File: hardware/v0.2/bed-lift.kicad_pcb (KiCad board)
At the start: 4 copper layers, 175 x 40 mm, 113 parts, among them J1 SM04B-SRSS-TB, J10 S4B-XH-A, J11 S4B-XH-A, J12 S4B-XH-A, J13 S4B-XH-A, J2 S2P-VH, J3 SM04B-SRSS-TB, J4 TC2030-NL, J5 PH1-06-UA, J6 S3B-XH-A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

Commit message: Finalize for production
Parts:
- added TH1: JLCPCB_PCBA_Tooling_Hole, Generic:JLCPCB_PCBA_Tooling_Hole, F.Cu at (196.5, 61.8)
- added TH1: JLCPCB_PCBA_Tooling_Hole, Generic:JLCPCB_PCBA_Tooling_Hole, F.Cu at (36.5, 98.8)
- added TH1: JLCPCB_PCBA_Tooling_Hole, Generic:JLCPCB_PCBA_Tooling_Hole, F.Cu at (202.5, 92.8)
- added TH1: JLCPCB_PCBA_Tooling_Hole, Generic:JLCPCB_PCBA_Tooling_Hole, F.Cu at (61.8, 61.8)
- moved C1 6.75 mm to (39.0, 78.0)
- moved C2 6.75 mm to (42.5, 78.0)
- moved C7 2.00 mm to (47.8, 70.5)
- moved U2 1.25 mm to (40.8, 74.0), turned to 180 degrees
- moved R1 0.50 mm to (47.8, 74.8), turned to 90 degrees
- moved R2 0.50 mm to (45.8, 74.8), turned to 90 degrees
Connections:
- U2 pad 1: /BUS_3V3 -> +3.3V
- U2 pad 2: /BUS_SDA -> /I2C1_SDA
- U2 pad 3: /BUS_SCL -> /I2C1_SCL
- U2 pad 4: /BUS_GND -> GND
- U2 pad 5: GND -> /BUS_GND
- U2 pad 6: /I2C1_SCL -> /BUS_SCL
- U2 pad 7: /I2C1_SDA -> /BUS_SDA
- U2 pad 8: +3.3V -> /BUS_3V3
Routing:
- net +3.3V: track 297.9 -> 305.8 mm, vias 2 -> 3
- net /BUS_SCL: track 16.2 -> 18.9 mm, vias 2 -> 3
- net /BUS_GND: track 23.1 -> 20.4 mm
- net /~{RESET}: track 36.9 -> 35.7 mm
- net /BUS_SDA: track 15.7 -> 16.7 mm, vias 2 -> 3
- net GND: track 124.2 -> 123.2 mm, vias 476 -> 477
- net /LIFT1_HALL2: track 51.3 -> 50.3 mm
- net /LIFT1_HALL1: track 49.9 -> 48.9 mm
- net /I2C1_SDA: track 9.67 -> 9.08 mm
- net /LIFT2_IN2: track 69.0 -> 68.4 mm
- net /LIFT2_HALL1: track 81.1 -> 80.5 mm
- net /LIFT2_IN1: track 71.7 -> 71.1 mm
- net /LIFT2_HALL2: track 82.5 -> 81.9 mm
- net /I2C1_SCL: track 9.66 -> 9.29 mm, vias 2 -> 0

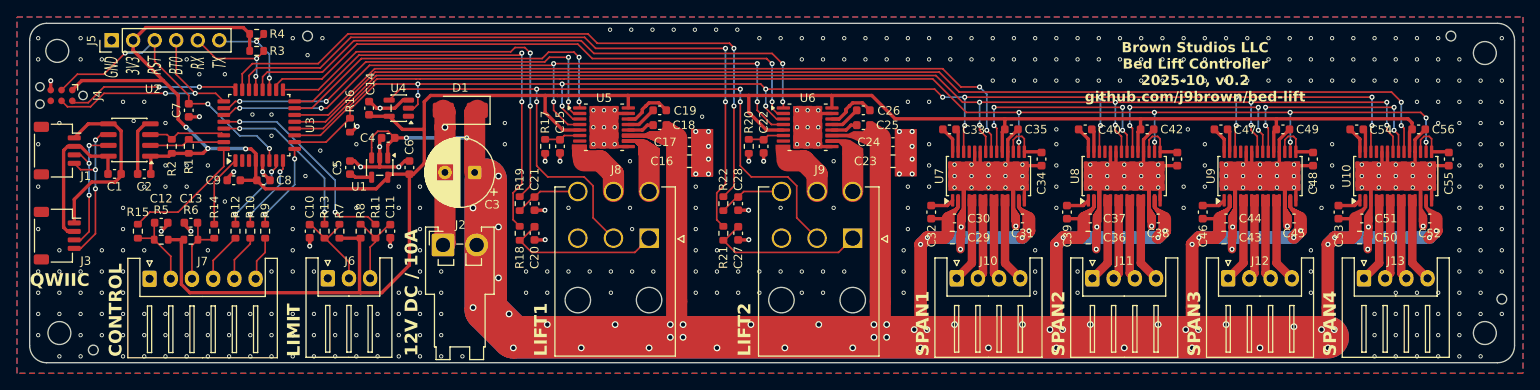
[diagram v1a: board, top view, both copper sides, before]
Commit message: Fix errata in v0.2, reversed lift motor pins 2 and 3.
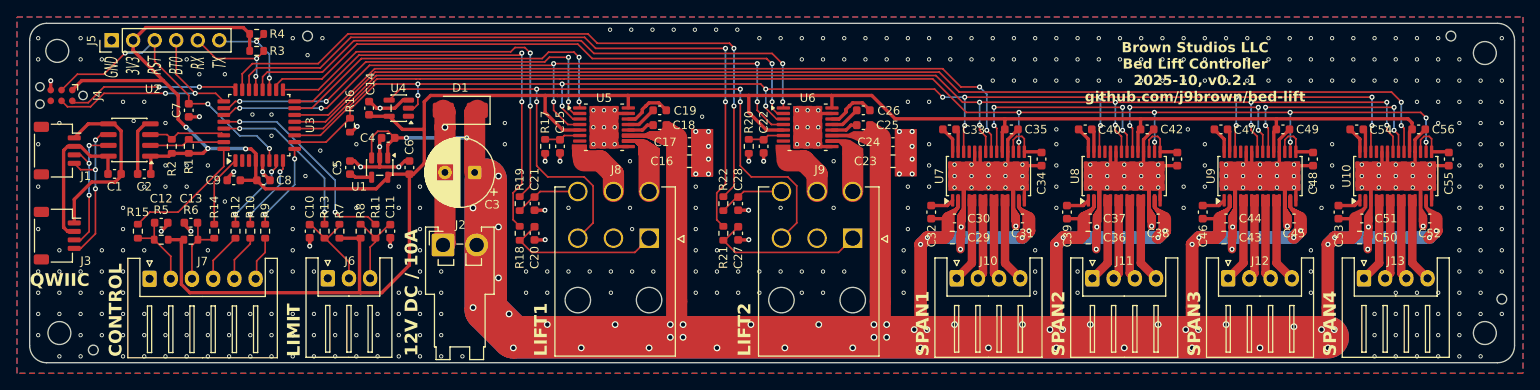
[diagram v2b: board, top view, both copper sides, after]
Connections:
- J8 pad 2: /VHALL -> GND
- J8 pad 3: GND -> /VHALL
- J9 pad 2: /VHALL -> GND
- J9 pad 3: GND -> /VHALL
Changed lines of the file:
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@@
 		(title "Bed Lift Controller")
 		(date "2025-10")
-		(rev "v0.2")
+		(rev "v0.2.1")
 		(company "Brown Studios LLC")
 		(comment 1 "github.com/j9brown/bed-lift")
@@
 			(layers "*.Cu")
 			(remove_unused_layers no)
-			(net 43 "/VHALL")
+			(net 1 "GND")
 			(pinfunction "Pin_2")
 			(pintype "passive")
@@
 			(layers "*.Cu")
 			(remove_unused_layers no)
-			(net 1 "GND")
+			(net 43 "/VHALL")
 			(pinfunction "Pin_3")
 			(pintype "passive")
@@
 			(layers "*.Cu")
 			(remove_unused_layers no)
-			(net 43 "/VHALL")
+			(net 1 "GND")
 			(pinfunction "Pin_2")
 			(pintype "passive")
@@
 			(layers "*.Cu")
 			(remove_unused_layers no)
-			(net 1 "GND")
+			(net 43 "/VHALL")
 			(pinfunction "Pin_3")
 			(pintype "passive")
@@
 			)
 		)
-		(property "Datasheet" "https://www.ti.com/lit/ds/symlink/iso1641.pdf"
+		(property "Datasheet" "https://www.ti.com/lit/ds/symlink/iso1640.pdf"
 			(at 0 0 0)
 			(layer "F.Fab")
@@
 	)
 	(segment
-		(start 77.943 75.75)
+		(start 77.943 77.8215)
 		(end 77.943 75.25)
 		(width 2.5)
@@
 	)
 	(segment
-		(start 77.943 77.8215)
-		(end 77.943 75.75)
-		(width 2.5)
-		(layer "F.Cu")
-		(net 1)
-	)
-	(segment
 		(start 123.55 70.875)
 		(end 122.0625 70.875)
@@
 	)
 	(segment
-		(start 95.4 83.17)
-		(end 95.4 79.4)
+		(start 112.75 68)
+		(end 88.75 68)
 		(width 0.2)
 		(layer "F.Cu")
@@
 	)
 	(segment
-		(start 112.75 68)
+		(start 72.662501 68)
 		(end 88.75 68)
 		(width 0.2)
@@
 	)
 	(segment
-		(start 72.662501 68)
-		(end 88.75 68)
+		(start 119.4 79.4)
+		(end 119.4 83.77)
 		(width 0.2)
 		(layer "F.Cu")
@@
 	)
 	(segment
-		(start 90.05 78.35)
-		(end 88.75 77.05)
+		(start 88.75 77.05)
+		(end 90.05 78.35)
 		(width 0.2)
 		(layer "F.Cu")
@@
 	)
 	(segment
-		(start 112.75 77.05)
-		(end 112.75 69.5)
+		(start 94.35 78.35)
+		(end 95.4 79.4)
 		(width 0.2)
 		(layer "F.Cu")
@@
 	(segment
 		(start 118.35 78.35)
-		(end 114.05 78.35)
+		(end 119.4 79.4)
 		(width 0.2)
 		(layer "F.Cu")
@@
 	)
 	(segment
-		(start 121.8 85.57)
-		(end 119.4 83.17)
+		(start 119.4 83.77)
+		(end 117.6 85.57)
 		(width 0.2)
 		(layer "F.Cu")
@@
 	)
 	(segment
-		(start 114.05 78.35)
-		(end 112.75 77.05)
+		(start 90.05 78.35)
+		(end 94.35 78.35)
 		(width 0.2)
 		(layer "F.Cu")
@@
 	)
 	(segment
-		(start 94.35 78.35)
-		(end 90.05 78.35)
+		(start 112.75 77.05)
+		(end 114.05 78.35)
 		(width 0.2)
 		(layer "F.Cu")
@@
 	)
 	(segment
-		(start 97.8 85.57)
-		(end 95.4 83.17)
+		(start 95.4 79.4)
+		(end 95.4 83.77)
 		(width 0.2)
 		(layer "F.Cu")
@@
 	)
 	(segment
-		(start 88.75 77.05)
-		(end 88.75 69.5)
+		(start 114.05 78.35)
+		(end 118.35 78.35)
 		(width 0.2)
 		(layer "F.Cu")
@@
 	)
 	(segment
-		(start 119.4 83.17)
-		(end 119.4 79.4)
+		(start 88.75 69.5)
+		(end 88.75 77.05)
 		(width 0.2)
 		(layer "F.Cu")
@@
 	)
 	(segment
-		(start 71.3625 69.300001)
-		(end 72.662501 68)
+		(start 112.75 69.5)
+		(end 112.75 77.05)
 		(width 0.2)
 		(layer "F.Cu")
@@
 	)
 	(segment
-		(start 95.4 79.4)
-		(end 94.35 78.35)
+		(start 95.4 83.77)
+		(end 93.6 85.57)
 		(width 0.2)
 		(layer "F.Cu")
@@
 	)
 	(segment
-		(start 119.4 79.4)
-		(end 118.35 78.35)
+		(start 71.3625 69.300001)
+		(end 72.662501 68)
 		(width 0.2)
 		(layer "F.Cu")
@@
 	)
 	(segment
-		(start 69.300001 76.1125)
-		(end 69.3 74.9)
+		(start 69.3 73.69989)
+		(end 69.300001 76.1125)
 		(width 0.2)
 		(layer "F.Cu")
@@
 		(width 0.2)
 		(layer "F.Cu")
-		(net 103)
-	)
-	(segment
-		(start 69.3 74.9)
-		(end 69.3 73.69989)
-		(width 0.2)
-		(layer "F.Cu")
